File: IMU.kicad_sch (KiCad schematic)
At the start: 9 parts, among them U2 BNO055, U3 LIS3MDL

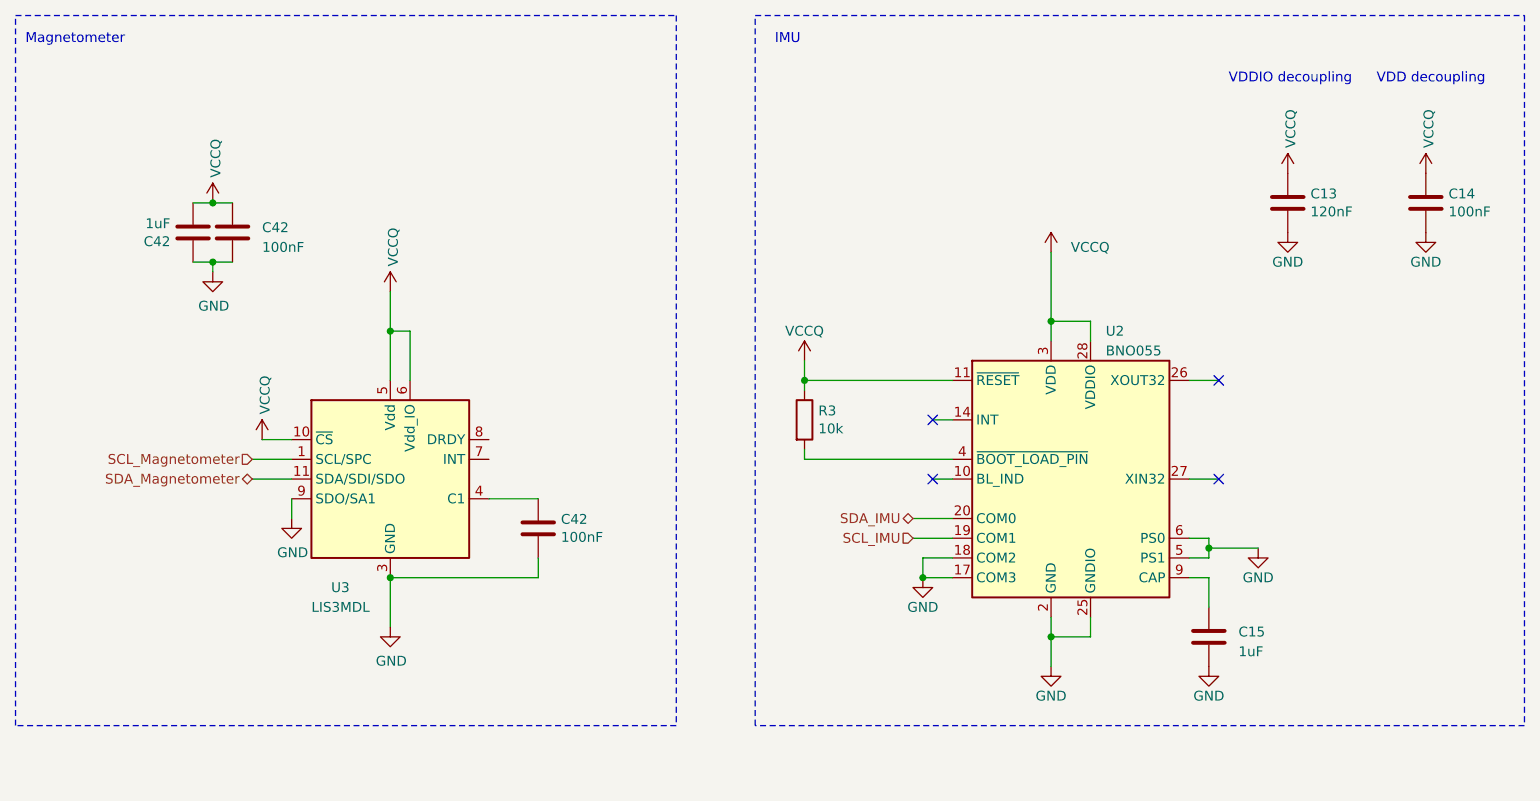
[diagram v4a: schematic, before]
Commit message: Reannotate schematic
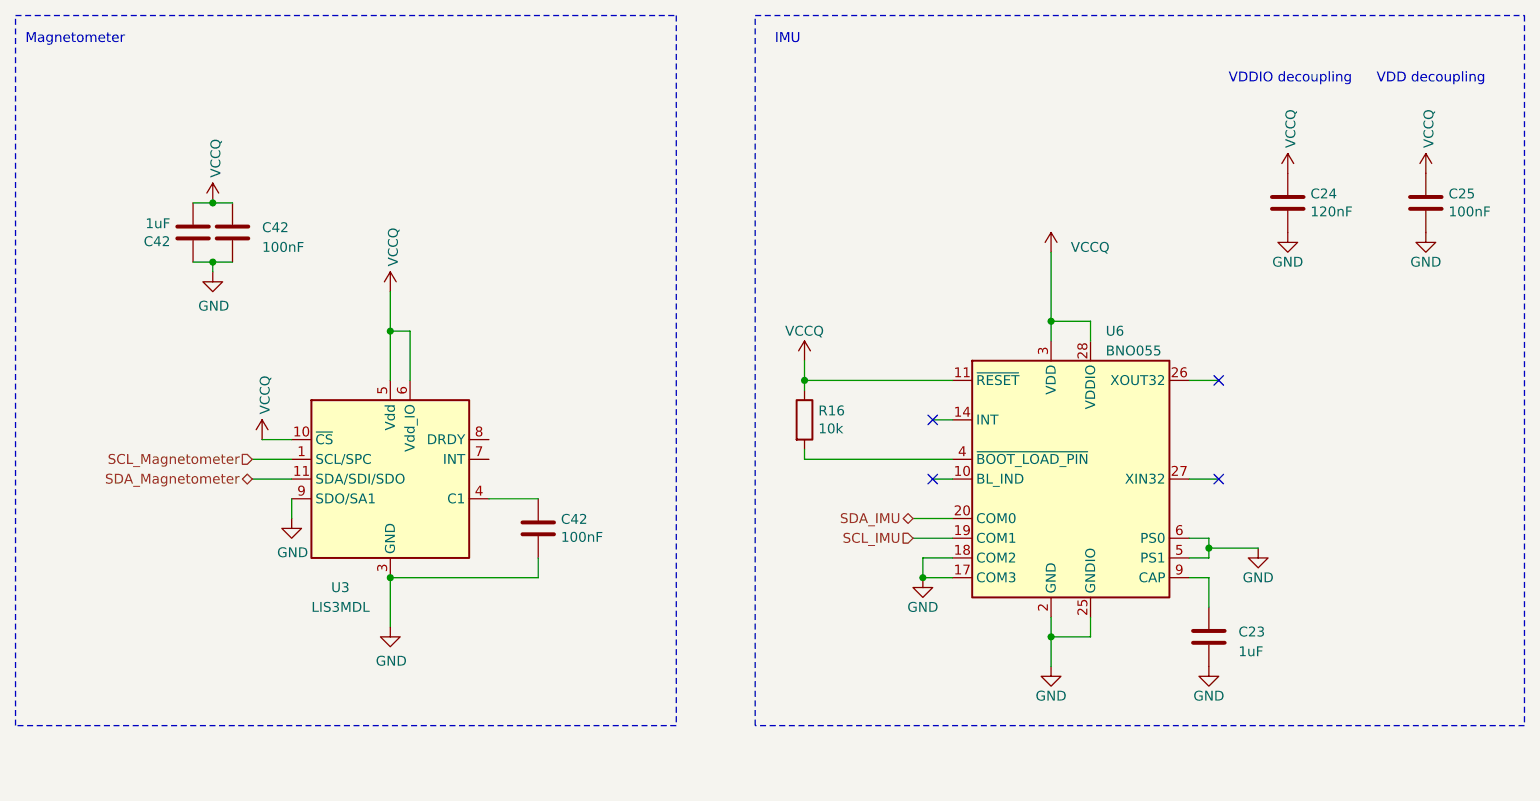
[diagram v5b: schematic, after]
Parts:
- renumbered C15 to C23, C13 to C24, C14 to C25, R3 to R16, U2 to U6
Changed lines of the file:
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@@
   (symbol (lib_id "power:GND") (at 168.91 97.79 0) (unit 1)
     (in_bom yes) (on_board yes) (dnp no)
-    (property "Reference" "#PWR048" (at 168.91 104.14 0)
+    (property "Reference" "#PWR070" (at 168.91 104.14 0)
       (effects (font (size 1.27 1.27)) hide)
     )
@@
       (project "NEW_PCB_ADCS"
         (path "/42c40d7d-71af-4ce9-bac9-d638f259c957/ba04218b-8bf3-443f-b78c-44dd521550b8"
-          (reference "#PWR048") (unit 1)
+          (reference "#PWR070") (unit 1)
         )
       )
@@
       (project "NEW_PCB_ADCS"
         (path "/42c40d7d-71af-4ce9-bac9-d638f259c957/ba04218b-8bf3-443f-b78c-44dd521550b8"
-          (reference "U1") (unit 1)
+          (reference "U5") (unit 1)
         )
       )
@@
       (project "NEW_PCB_ADCS"
         (path "/42c40d7d-71af-4ce9-bac9-d638f259c957/ba04218b-8bf3-443f-b78c-44dd521550b8"
-          (reference "C19") (unit 1)
+          (reference "C21") (unit 1)
         )
       )
@@
         )
         (path "/42c40d7d-71af-4ce9-bac9-d638f259c957/ba04218b-8bf3-443f-b78c-44dd521550b8"
-          (reference "#PWR036") (unit 1)
+          (reference "#PWR066") (unit 1)
         )
       )
@@
         )
         (path "/42c40d7d-71af-4ce9-bac9-d638f259c957/ba04218b-8bf3-443f-b78c-44dd521550b8"
-          (reference "#PWR044") (unit 1)
+          (reference "#PWR077") (unit 1)
         )
       )
@@
         )
         (path "/42c40d7d-71af-4ce9-bac9-d638f259c957/ba04218b-8bf3-443f-b78c-44dd521550b8"
-          (reference "#PWR041") (unit 1)
+          (reference "#PWR075") (unit 1)
         )
       )
@@
         )
         (path "/42c40d7d-71af-4ce9-bac9-d638f259c957/ba04218b-8bf3-443f-b78c-44dd521550b8"
-          (reference "#PWR049") (unit 1)
+          (reference "#PWR069") (unit 1)
         )
       )
@@
         )
         (path "/42c40d7d-71af-4ce9-bac9-d638f259c957/ba04218b-8bf3-443f-b78c-44dd521550b8"
-          (reference "#PWR027") (unit 1)
+          (reference "#PWR063") (unit 1)
         )
       )
@@
   (symbol (lib_id "power:GND") (at 233.68 53.34 0) (unit 1)
     (in_bom yes) (on_board yes) (dnp no)
-    (property "Reference" "#PWR043" (at 233.68 59.69 0)
+    (property "Reference" "#PWR078" (at 233.68 59.69 0)
       (effects (font (size 1.27 1.27)) hide)
     )
@@
       (project "NEW_PCB_ADCS"
         (path "/42c40d7d-71af-4ce9-bac9-d638f259c957/ba04218b-8bf3-443f-b78c-44dd521550b8"
-          (reference "#PWR043") (unit 1)
+          (reference "#PWR078") (unit 1)
         )
       )
@@
         )
         (path "/42c40d7d-71af-4ce9-bac9-d638f259c957/ba04218b-8bf3-443f-b78c-44dd521550b8"
-          (reference "#PWR040") (unit 1)
+          (reference "#PWR068") (unit 1)
         )
       )
@@
       (project "NEW_PCB_ADCS"
         (path "/42c40d7d-71af-4ce9-bac9-d638f259c957/ba04218b-8bf3-443f-b78c-44dd521550b8"
-          (reference "C20") (unit 1)
+          (reference "C22") (unit 1)
         )
       )
@@
   (symbol (lib_id "power:GND") (at 185.42 109.22 0) (unit 1)
     (in_bom yes) (on_board yes) (dnp no)
-    (property "Reference" "#PWR033" (at 185.42 115.57 0)
+    (property "Reference" "#PWR072" (at 185.42 115.57 0)
       (effects (font (size 1.27 1.27)) hide)
     )
@@
       (project "NEW_PCB_ADCS"
         (path "/42c40d7d-71af-4ce9-bac9-d638f259c957/ba04218b-8bf3-443f-b78c-44dd521550b8"
-          (reference "#PWR033") (unit 1)
+          (reference "#PWR072") (unit 1)
         )
       )
@@
         )
         (path "/42c40d7d-71af-4ce9-bac9-d638f259c957/ba04218b-8bf3-443f-b78c-44dd521550b8"
-          (reference "#PWR035") (unit 1)
+          (reference "#PWR065") (unit 1)
         )
       )
@@
   (symbol (lib_id "power:GND") (at 212.09 93.98 0) (unit 1)
     (in_bom yes) (on_board yes) (dnp no)
-    (property "Reference" "#PWR045" (at 212.09 100.33 0)
+    (property "Reference" "#PWR074" (at 212.09 100.33 0)
       (effects (font (size 1.27 1.27)) hide)
     )
@@
       (project "NEW_PCB_ADCS"
         (path "/42c40d7d-71af-4ce9-bac9-d638f259c957/ba04218b-8bf3-443f-b78c-44dd521550b8"
-          (reference "#PWR045") (unit 1)
+          (reference "#PWR074") (unit 1)
         )
       )
@@
   (symbol (lib_id "Sensor_Motion:BNO055") (at 187.96 85.09 0) (unit 1)
     (in_bom yes) (on_board yes) (dnp no) (fields_autoplaced)
-    (property "Reference" "U2" (at 192.4559 66.04 0)
+    (property "Reference" "U6" (at 192.4559 66.04 0)
       (effects (font (size 1.27 1.27)) (justify left))
     )
@@
       (project "NEW_PCB_ADCS"
         (path "/42c40d7d-71af-4ce9-bac9-d638f259c957/ba04218b-8bf3-443f-b78c-44dd521550b8"
-          (reference "U2") (unit 1)
+          (reference "U6") (unit 1)
         )
       )
@@
   (symbol (lib_id "Device:C") (at 205.74 105.41 0) (unit 1)
     (in_bom yes) (on_board yes) (dnp no) (fields_autoplaced)
-    (property "Reference" "C15" (at 209.55 104.775 0)
+    (property "Reference" "C23" (at 209.55 104.775 0)
       (effects (font (size 1.27 1.27)) (justify left))
     )
@@
       (project "NEW_PCB_ADCS"
         (path "/42c40d7d-71af-4ce9-bac9-d638f259c957/ba04218b-8bf3-443f-b78c-44dd521550b8"
-          (reference "C15") (unit 1)
+          (reference "C23") (unit 1)
         )
       )
@@
   (symbol (lib_id "power:GND") (at 215.9 53.34 0) (unit 1)
     (in_bom yes) (on_board yes) (dnp no)
-    (property "Reference" "#PWR042" (at 215.9 59.69 0)
+    (property "Reference" "#PWR076" (at 215.9 59.69 0)
       (effects (font (size 1.27 1.27)) hide)
     )
@@
       (project "NEW_PCB_ADCS"
         (path "/42c40d7d-71af-4ce9-bac9-d638f259c957/ba04218b-8bf3-443f-b78c-44dd521550b8"
-          (reference "#PWR042") (unit 1)
+          (reference "#PWR076") (unit 1)
         )
       )
@@
         )
         (path "/42c40d7d-71af-4ce9-bac9-d638f259c957/ba04218b-8bf3-443f-b78c-44dd521550b8"
-          (reference "#PWR032") (unit 1)
+          (reference "#PWR064") (unit 1)
         )
       )
@@
   (symbol (lib_id "Device:R") (at 153.67 77.47 0) (unit 1)
     (in_bom yes) (on_board yes) (dnp no)
-    (property "Reference" "R3" (at 155.448 76.3016 0)
+    (property "Reference" "R16" (at 155.448 76.3016 0)
       (effects (font (size 1.27 1.27)) (justify left))
     )
@@
       (project "NEW_PCB_ADCS"
         (path "/42c40d7d-71af-4ce9-bac9-d638f259c957/ba04218b-8bf3-443f-b78c-44dd521550b8"
-          (reference "R3") (unit 1)
+          (reference "R16") (unit 1)
         )
       )
@@
   (symbol (lib_id "Device:C") (at 215.9 49.53 0) (unit 1)
     (in_bom yes) (on_board yes) (dnp no)
-    (property "Reference" "C13" (at 218.821 48.3616 0)
+    (property "Reference" "C24" (at 218.821 48.3616 0)
       (effects (font (size 1.27 1.27)) (justify left))
     )
@@
       (project "NEW_PCB_ADCS"
         (path "/42c40d7d-71af-4ce9-bac9-d638f259c957/ba04218b-8bf3-443f-b78c-44dd521550b8"
-          (reference "C13") (unit 1)
+          (reference "C24") (unit 1)
         )
       )
@@
       (project "NEW_PCB_ADCS"
         (path "/42c40d7d-71af-4ce9-bac9-d638f259c957/ba04218b-8bf3-443f-b78c-44dd521550b8"
-          (reference "C18") (unit 1)
+          (reference "C20") (unit 1)
         )
       )
@@
         )
         (path "/42c40d7d-71af-4ce9-bac9-d638f259c957/ba04218b-8bf3-443f-b78c-44dd521550b8"
-          (reference "#PWR037") (unit 1)
+          (reference "#PWR067") (unit 1)
         )
       )
@@
         )
         (path "/42c40d7d-71af-4ce9-bac9-d638f259c957/ba04218b-8bf3-443f-b78c-44dd521550b8"
-          (reference "#PWR034") (unit 1)
+          (reference "#PWR071") (unit 1)
         )
       )
@@
   (symbol (lib_id "Device:C") (at 233.68 49.53 0) (unit 1)
     (in_bom yes) (on_board yes) (dnp no)
-    (property "Reference" "C14" (at 236.601 48.3616 0)
+    (property "Reference" "C25" (at 236.601 48.3616 0)
       (effects (font (size 1.27 1.27)) (justify left))
     )
@@
       (project "NEW_PCB_ADCS"
         (path "/42c40d7d-71af-4ce9-bac9-d638f259c957/ba04218b-8bf3-443f-b78c-44dd521550b8"
-          (reference "C14") (unit 1)
+          (reference "C25") (unit 1)
         )
       )
@@
   (symbol (lib_id "power:GND") (at 205.74 109.22 0) (unit 1)
     (in_bom yes) (on_board yes) (dnp no)
-    (property "Reference" "#PWR051" (at 205.74 115.57 0)
+    (property "Reference" "#PWR073" (at 205.74 115.57 0)
       (effects (font (size 1.27 1.27)) hide)
     )
@@
       (project "NEW_PCB_ADCS"
         (path "/42c40d7d-71af-4ce9-bac9-d638f259c957/ba04218b-8bf3-443f-b78c-44dd521550b8"
-          (reference "#PWR051") (unit 1)
-        )
-      )
+          (reference "#PWR073") (unit 1)
+        )
+      )

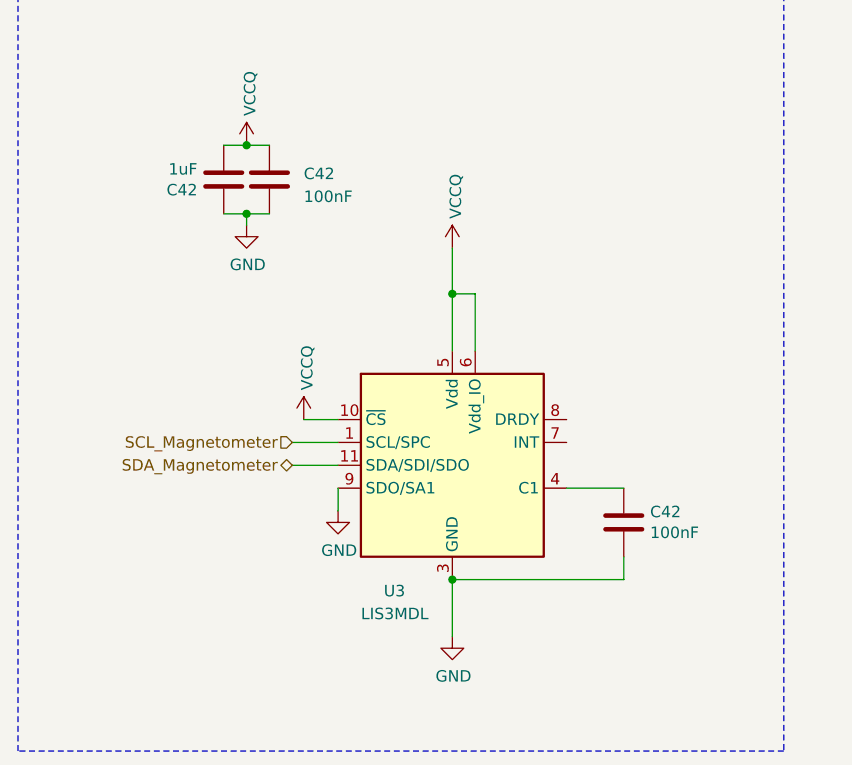
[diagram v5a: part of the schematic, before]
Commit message: Create PCB layout and routing
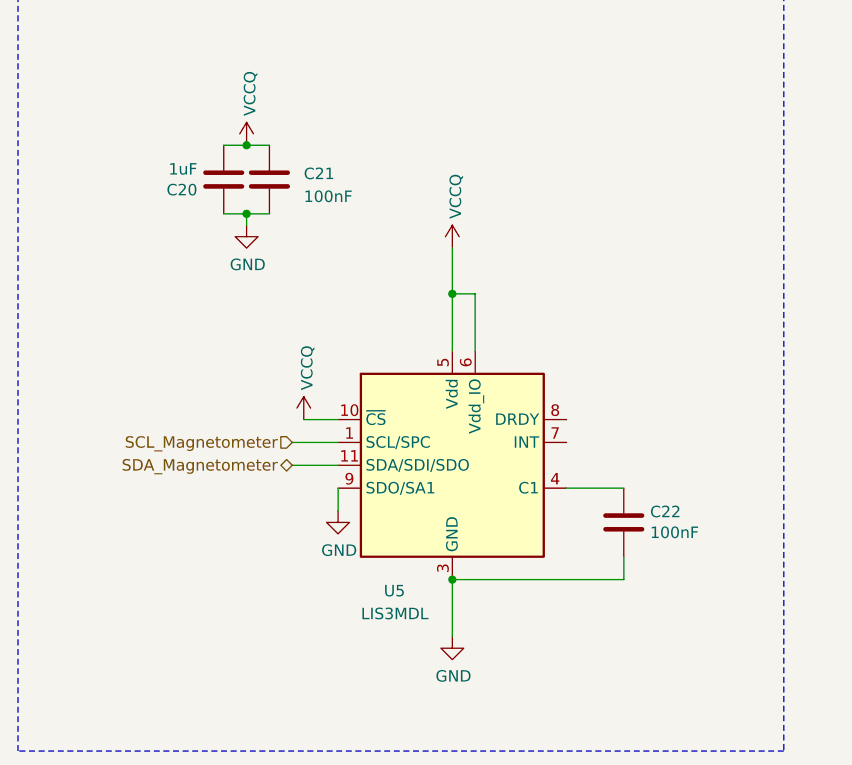
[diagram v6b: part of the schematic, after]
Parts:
- C23: footprint (none) -> Capacitor_SMD:C_0603_1608Metric
- R16: footprint Resistor_SMD:R_0603_1608Metric_Pad1.05x0.95mm_HandSolder -> Resistor_SMD:R_0603_1608Metric
- renumbered C42 to C20, C42 to C21, C42 to C22, U3 to U5
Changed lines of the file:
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@@
   (symbol (lib_id "Sensor_Magnetic:LIS3MDL") (at 100.33 85.09 0) (unit 1)
     (in_bom yes) (on_board yes) (dnp no)
-    (property "Reference" "U3" (at 92.71 99.06 0)
+    (property "Reference" "U5" (at 92.71 99.06 0)
       (effects (font (size 1.27 1.27)) (justify left))
     )
@@
   (symbol (lib_id "Device:C") (at 80.01 53.34 180) (unit 1)
     (in_bom yes) (on_board yes) (dnp no) (fields_autoplaced)
-    (property "Reference" "C42" (at 83.82 52.705 0)
+    (property "Reference" "C21" (at 83.82 52.705 0)
       (effects (font (size 1.27 1.27)) (justify right))
     )
@@
   (symbol (lib_id "Device:C") (at 119.38 91.44 0) (unit 1)
     (in_bom yes) (on_board yes) (dnp no)
-    (property "Reference" "C42" (at 122.301 90.2716 0)
+    (property "Reference" "C22" (at 122.301 90.2716 0)
       (effects (font (size 1.27 1.27)) (justify left))
     )
@@
       (effects (font (size 1.27 1.27)) (justify left))
     )
-    (property "Footprint" "" (at 206.7052 109.22 0)
+    (property "Footprint" "Capacitor_SMD:C_0603_1608Metric" (at 206.7052 109.22 0)
       (effects (font (size 1.27 1.27)) hide)
     )
@@
       (effects (font (size 1.27 1.27)) (justify left))
     )
-    (property "Footprint" "Resistor_SMD:R_0603_1608Metric_Pad1.05x0.95mm_HandSolder" (at 151.892 77.47 90)
+    (property "Footprint" "Resistor_SMD:R_0603_1608Metric" (at 151.892 77.47 90)
       (effects (font (size 1.27 1.27)) hide)
     )
@@
   (symbol (lib_id "Device:C") (at 74.93 53.34 180) (unit 1)
     (in_bom yes) (on_board yes) (dnp no)
-    (property "Reference" "C42" (at 72.009 54.5084 0)
-      (effects (font (size 1.27 1.27)) (justify left))
-    )
+    (property "Reference" "C20" (at 72.009 54.5084 0)
+      (effects (font (size 1.27 1.27)) (justify left))
+    )

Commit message: Fix some issues
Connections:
- net +3V3 renamed VCCQ
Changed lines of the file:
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@@
     )
   )
-  (symbol (lib_id "power:+3.3V") (at 233.68 45.72 0) (unit 1)
+  (symbol (lib_id "power:VCCQ") (at 233.68 45.72 0) (unit 1)
     (in_bom yes) (on_board yes) (dnp no)
     (property "Reference" "#PWR023" (at 233.68 49.53 0)
@@
     )
   )
-  (symbol (lib_id "power:+3.3V") (at 215.9 45.72 0) (unit 1)
+  (symbol (lib_id "power:VCCQ") (at 215.9 45.72 0) (unit 1)
     (in_bom yes) (on_board yes) (dnp no)
     (property "Reference" "#PWR023" (at 215.9 49.53 0)
@@
     )
   )
-  (symbol (lib_id "power:+3.3V") (at 153.67 69.85 0) (unit 1)
+  (symbol (lib_id "power:VCCQ") (at 153.67 69.85 0) (unit 1)
     (in_bom yes) (on_board yes) (dnp no) (fields_autoplaced)
     (property "Reference" "#PWR023" (at 153.67 73.66 0)
@@
     )
   )
-  (symbol (lib_id "power:+3.3V") (at 77.47 49.53 0) (unit 1)
+  (symbol (lib_id "power:VCCQ") (at 77.47 49.53 0) (unit 1)
     (in_bom yes) (on_board yes) (dnp no)
     (property "Reference" "#PWR023" (at 77.47 53.34 0)
@@
     )
   )
-  (symbol (lib_id "power:+3.3V") (at 83.82 80.01 0) (unit 1)
+  (symbol (lib_id "power:VCCQ") (at 83.82 80.01 0) (unit 1)
     (in_bom yes) (on_board yes) (dnp no)
     (property "Reference" "#PWR023" (at 83.82 83.82 0)
@@
     )
   )
-  (symbol (lib_id "power:+3.3V") (at 100.33 60.96 0) (unit 1)
+  (symbol (lib_id "power:VCCQ") (at 100.33 60.96 0) (unit 1)
     (in_bom yes) (on_board yes) (dnp no)
     (property "Reference" "#PWR023" (at 100.33 64.77 0)
@@
     )
   )
-  (symbol (lib_id "power:+3.3V") (at 185.42 55.88 0) (unit 1)
+  (symbol (lib_id "power:VCCQ") (at 185.42 55.88 0) (unit 1)
     (in_bom yes) (on_board yes) (dnp no) (fields_autoplaced)
     (property "Reference" "#PWR023" (at 185.42 59.69 0)

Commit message: Update some part numbers
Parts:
- C23: Part Number (none) -> C0603C104K9RACTU
- C24: Part Number C0603C104K9RACTU -> C0603C124J4RACTU
- R16: MPN (none) -> RE0603BRE0710KL
- U5: Part Number (none) -> LIS3MDLTR
- U6: Part Number (none) -> BNO055
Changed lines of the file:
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@@
+      (effects (font (size 1.27 1.27)) hide)
+    )
+    (property "Part Number" "LIS3MDLTR" (at 100.33 85.09 0)
       (effects (font (size 1.27 1.27)) hide)
     )
@@
     )
     (property "Datasheet" "https://www.bosch-sensortec.com/media/boschsensortec/downloads/datasheets/bst-bno055-ds000.pdf" (at 187.96 63.5 0)
+      (effects (font (size 1.27 1.27)) hide)
+    )
+    (property "Part Number" "BNO055" (at 187.96 85.09 0)
       (effects (font (size 1.27 1.27)) hide)
     )
@@
       (effects (font (size 1.27 1.27)) hide)
     )
+    (property "Part Number" "C0603C104K9RACTU" (at 205.74 105.41 0)
+      (effects (font (size 1.27 1.27)) hide)
+    )
     (pin "1")
     (pin "2")
@@
       (effects (font (size 1.27 1.27)) hide)
     )
+    (property "MPN" "RE0603BRE0710KL" (at 153.67 77.47 0)
+      (effects (font (size 1.27 1.27)) hide)
+    )
     (pin "1")
     (pin "2")
@@
       (effects (font (size 1.27 1.27)) hide)
     )
-    (property "Part Number" "C0603C104K9RACTU" (at 215.9 49.53 0)
-      (effects (font (size 1.27 1.27)) hide)
-    )
+    (property "Part Number" "C0603C124J4RACTU" (at 215.9 49.53 0)
+      (effects (font (size 1.27 1.27)) hide)
+    )
